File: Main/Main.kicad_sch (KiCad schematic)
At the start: 56 parts, among them J1 Conn_02x16_Odd_Even, J2 TYPE-C 6P, Q3 S9013 J3(RANGE:200-350), SW2 SS-12D11G3R, U1 BQ24074RGT, U2 DRV8833PW, U3 HUSB237-AA001-DN06R, U4 RT9742GGJ5, U5 RT9742GGJ5, U6 INA219AxDCN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

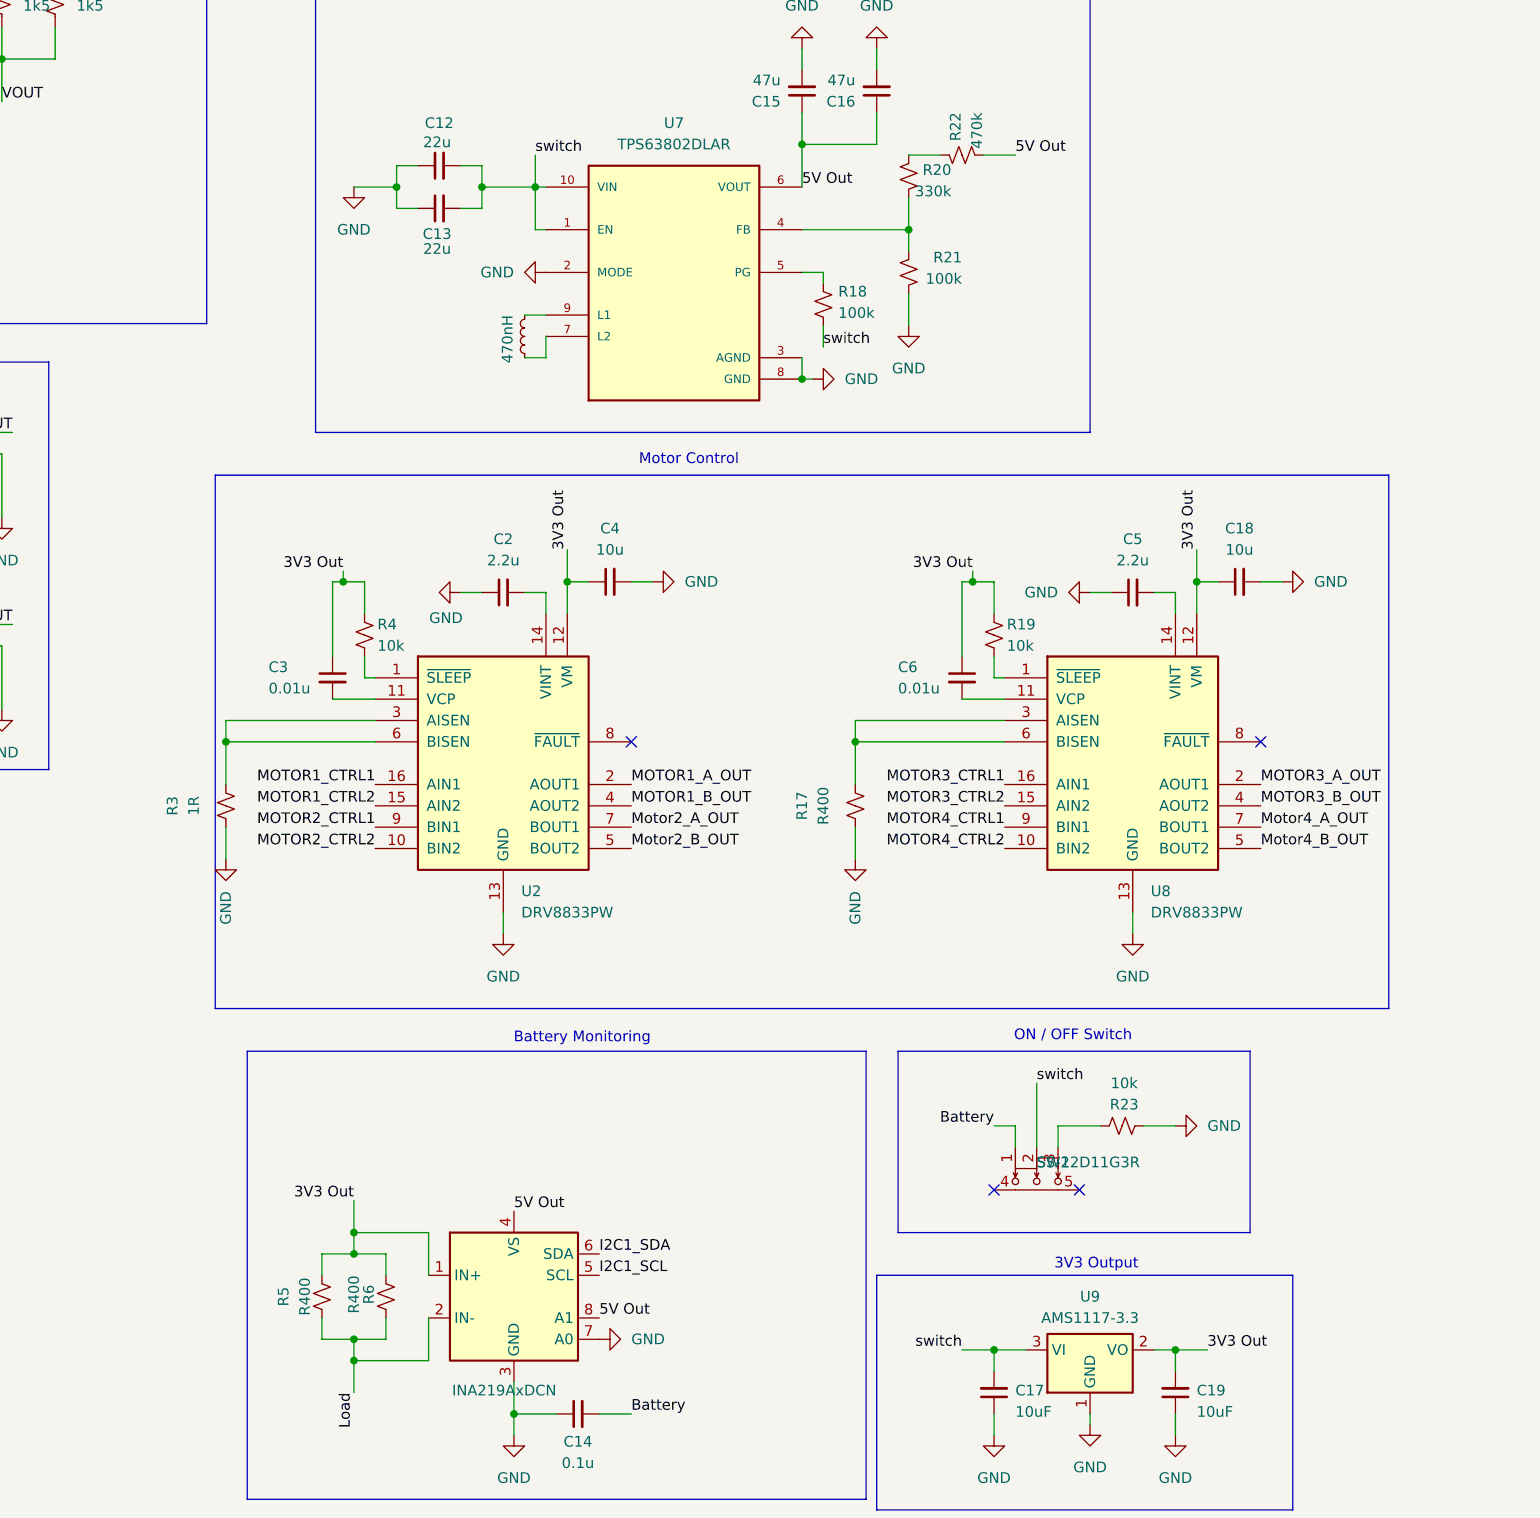
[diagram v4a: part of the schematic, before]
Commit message: Started PCB and Started Adding test points
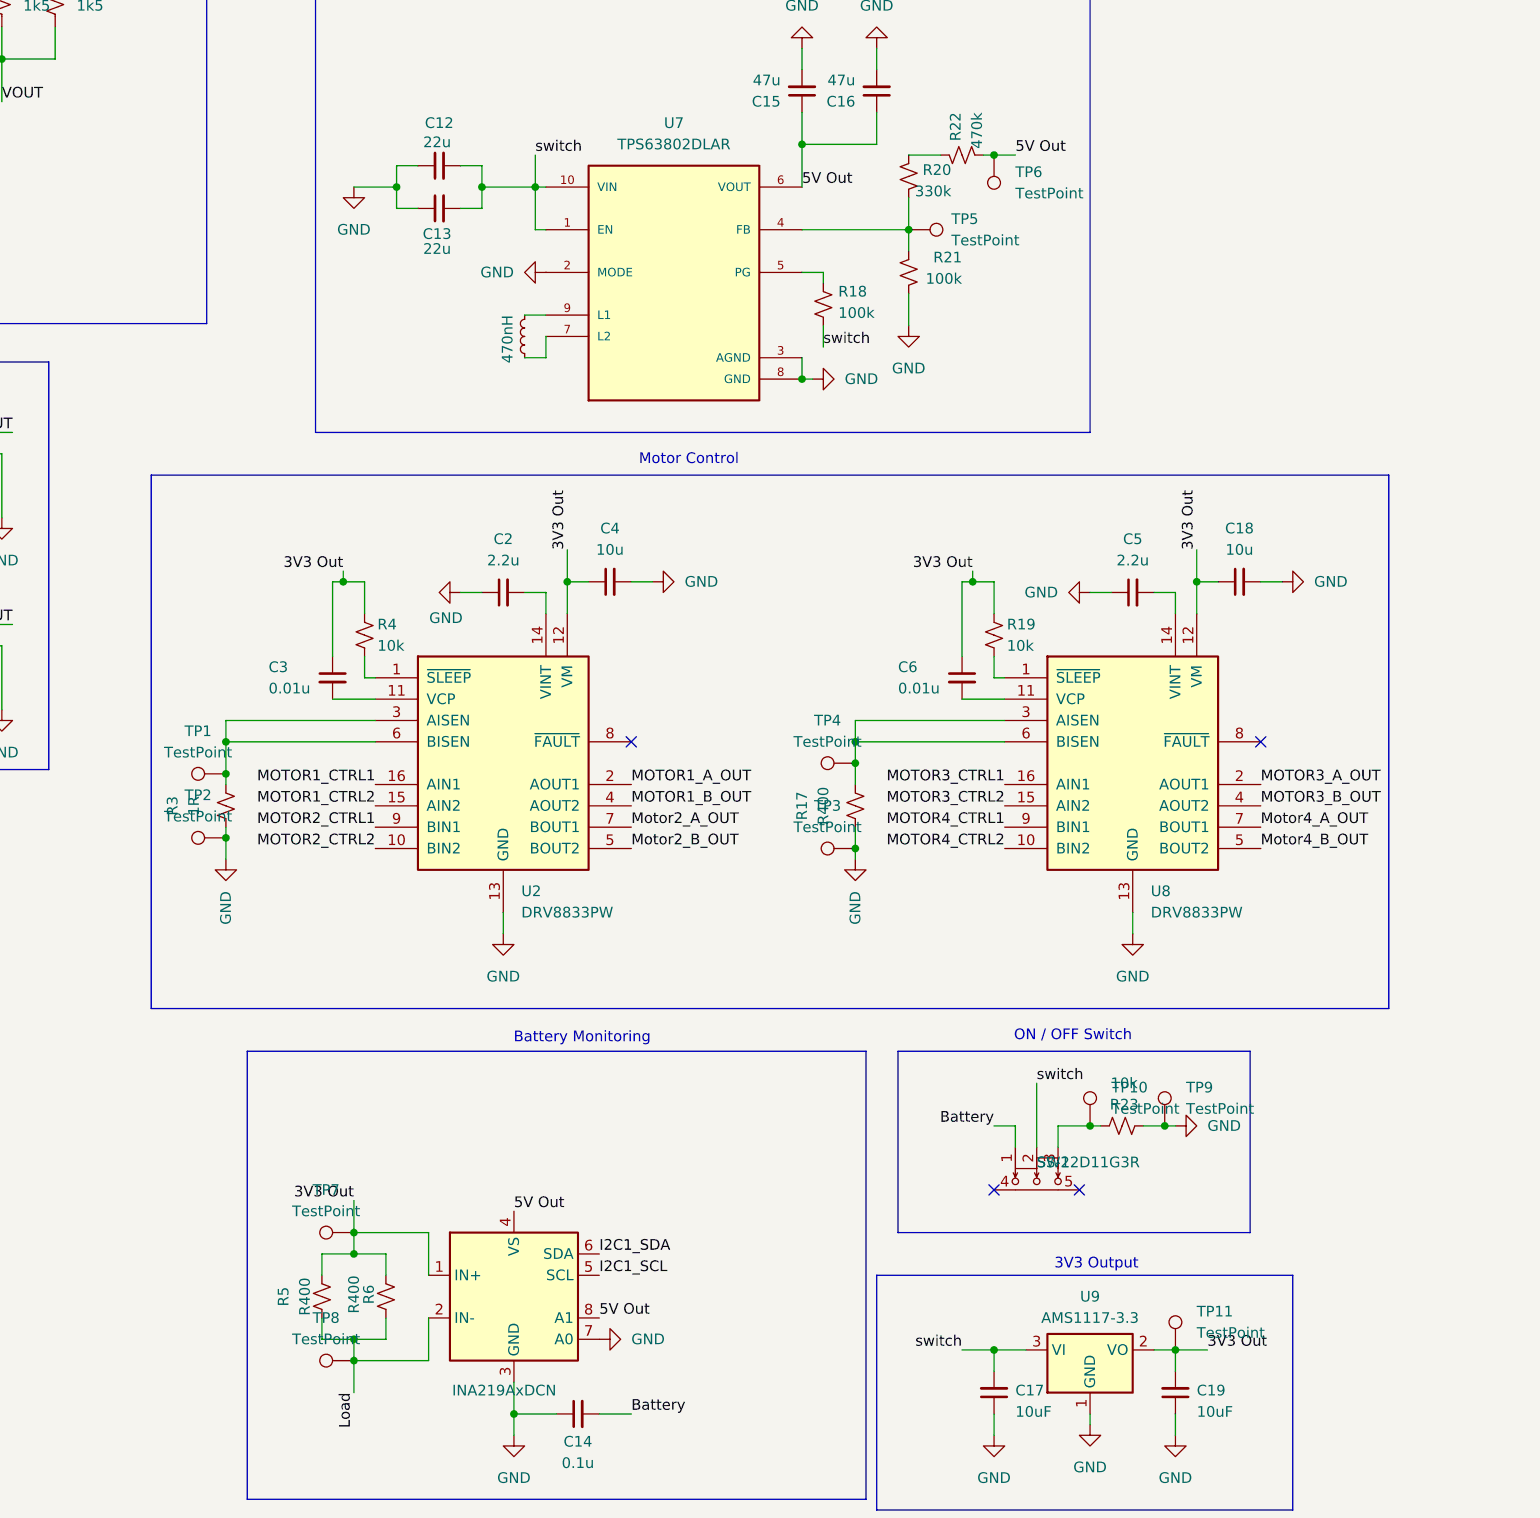
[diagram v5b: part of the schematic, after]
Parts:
- added TP1, TP10, TP11, TP2, TP3, TP4, TP5, TP6, TP7, TP8, TP9: TestPoint, symbol Connector:TestPoint
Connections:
- net 3V3 Out: now also TP11.1, TP7.1
- net 5V Out: now also TP6.1
- net GND: now also TP2.1, TP3.1, TP9.1
- net Load: now also TP8.1
- net at R20.2, R21.1, U7.4 (FB): now also TP5.1
- net at R23.2, SW2.3: now also TP10.1
- net at R17.2, U8.3 (AISEN), U8.6 (BISEN): now also TP4.1
- net at R3.2, U2.3 (AISEN), U2.6 (BISEN): now also TP1.1

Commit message: Got ALL the footprints present
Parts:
- TP1, TP10, TP11, TP2, TP3, TP4, TP5, TP6, TP7, TP8, TP9: footprint (none) -> TestPoint:TestPoint_Pad_D3.0mm
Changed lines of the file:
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@@
 			)
 		)
-		(property "Footprint" ""
+		(property "Footprint" "TestPoint:TestPoint_Pad_D3.0mm"
 			(at 140.97 213.36 0)
 			(effects
@@
 			)
 		)
-		(property "Footprint" ""
+		(property "Footprint" "TestPoint:TestPoint_Pad_D3.0mm"
 			(at 125.73 158.75 0)
 			(effects
@@
 			)
 		)
-		(property "Footprint" ""
+		(property "Footprint" "TestPoint:TestPoint_Pad_D3.0mm"
 			(at 200.66 157.48 0)
 			(effects
@@
 			)
 		)
-		(property "Footprint" ""
+		(property "Footprint" "TestPoint:TestPoint_Pad_D3.0mm"
 			(at 212.09 90.17 0)
 			(effects
@@
 			)
 		)
-		(property "Footprint" ""
+		(property "Footprint" "TestPoint:TestPoint_Pad_D3.0mm"
 			(at 242.57 205.74 0)
 			(effects
@@
 			)
 		)
-		(property "Footprint" ""
+		(property "Footprint" "TestPoint:TestPoint_Pad_D3.0mm"
 			(at 200.66 167.64 0)
 			(effects
@@
 			)
 		)
-		(property "Footprint" ""
+		(property "Footprint" "TestPoint:TestPoint_Pad_D3.0mm"
 			(at 243.84 232.41 0)
 			(effects
@@
 			)
 		)
-		(property "Footprint" ""
+		(property "Footprint" "TestPoint:TestPoint_Pad_D3.0mm"
 			(at 125.73 166.37 0)
 			(effects
@@
 			)
 		)
-		(property "Footprint" ""
+		(property "Footprint" "TestPoint:TestPoint_Pad_D3.0mm"
 			(at 233.68 205.74 0)
 			(effects
@@
 			)
 		)
-		(property "Footprint" ""
+		(property "Footprint" "TestPoint:TestPoint_Pad_D3.0mm"
 			(at 207.01 104.14 0)
 			(effects
@@
 			)
 		)
-		(property "Footprint" ""
+		(property "Footprint" "TestPoint:TestPoint_Pad_D3.0mm"
 			(at 140.97 228.6 0)
 			(effects
